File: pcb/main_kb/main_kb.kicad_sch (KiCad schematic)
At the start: 23 parts, among them J1 AVR-ISP-6, J2 TYPE-C-31-M-12, U1 ATMEGA32U4-AU

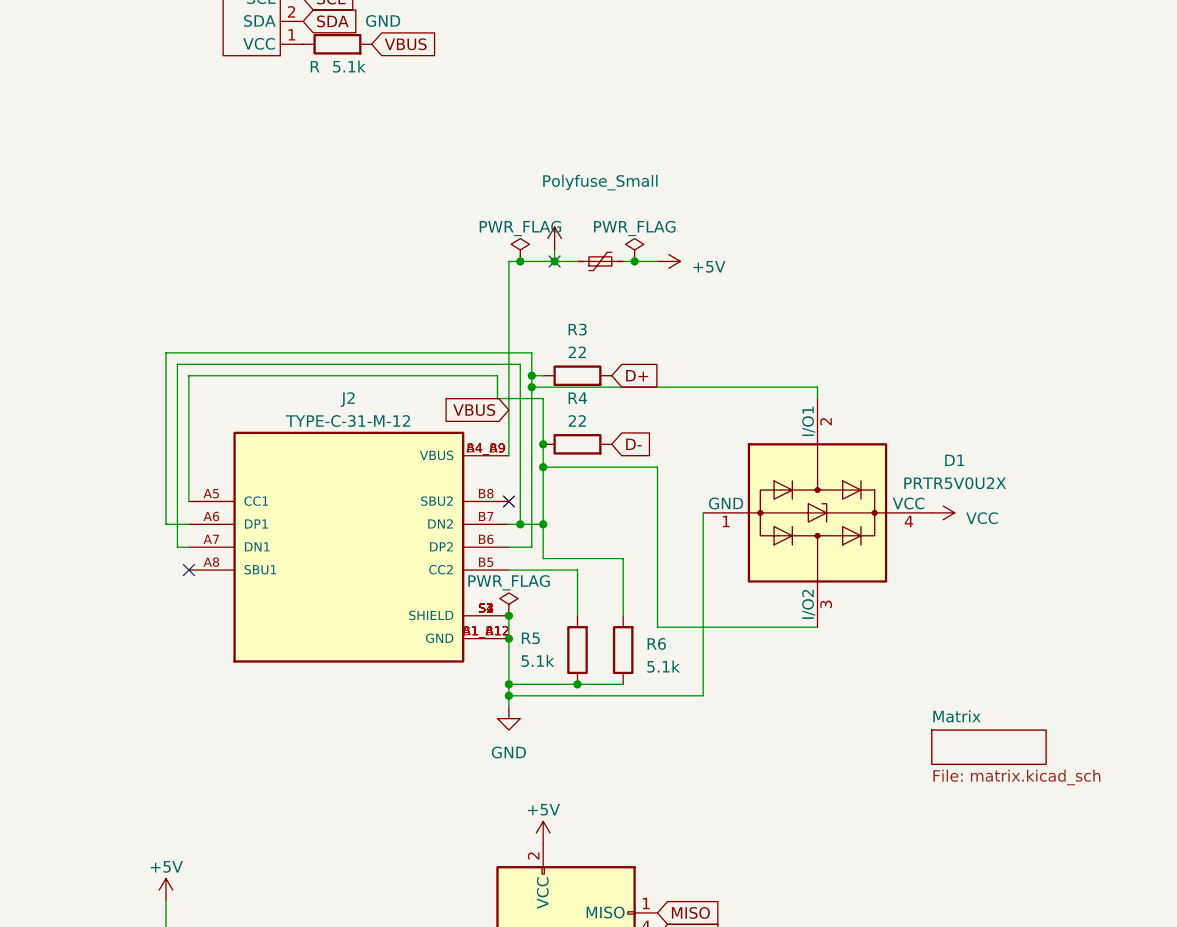
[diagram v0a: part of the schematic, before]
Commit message: Fixed type C Mess
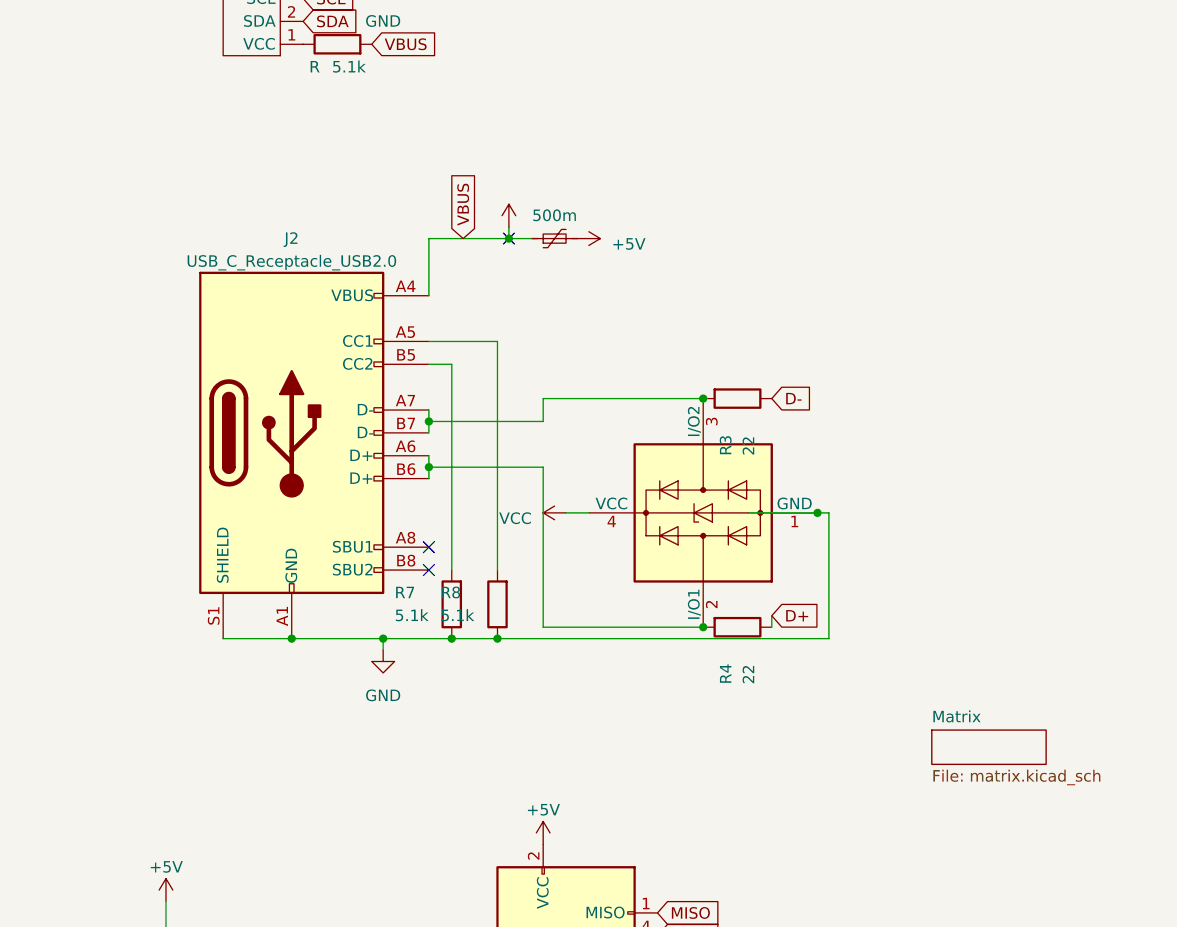
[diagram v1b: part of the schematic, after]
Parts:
- removed J2: TYPE-C-31-M-12, HRO_TYPE-C-31-M-12, symbol TYPE-C-31-M-12:TYPE-C-31-M-12
- removed R5, R6: 5.1k, symbol Device:R
- added J2: USB_C_Receptacle_USB2.0, Connector_USB:USB_C_Receptacle_G-Switch_GT-USB-7010ASV, symbol Connector:USB_C_Receptacle_USB2.0
- added R7, R8: 5.1k, symbol Device:R
- F1: value Polyfuse_Small -> 500m
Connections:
- net D+: now also R4.1; no longer R3.2
- net D-: now also R3.1; no longer R4.2
- net GND: now also J2.A1 (GND), J2.A12 (GND), J2.B1 (GND), J2.B12 (GND), J2.S1 (SHIELD), R7.1, R8.1
- net VCC: now also J2.A4 (VBUS), J2.A9 (VBUS), J2.B4 (VBUS), J2.B9 (VBUS)
- net at D1.2 (I/O1): now also R4.2, J2.A6 (D+), J2.B6 (D+); no longer R3.1
- net at D1.3 (I/O2): now also R3.2, J2.A7 (D-), J2.B7 (D-); no longer R4.1
- new net: J2.B5 (CC2), R7.2
- new net: J2.A5 (CC1), R8.2
